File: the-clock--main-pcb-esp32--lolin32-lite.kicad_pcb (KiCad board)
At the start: 2 copper layers, 101.6 x 38.1 mm, 19 parts, among them J1 Conn_01x04, SW1 SW_Push, SW2 SW_Push, SW3 SW_Push, SW4 SW_Push

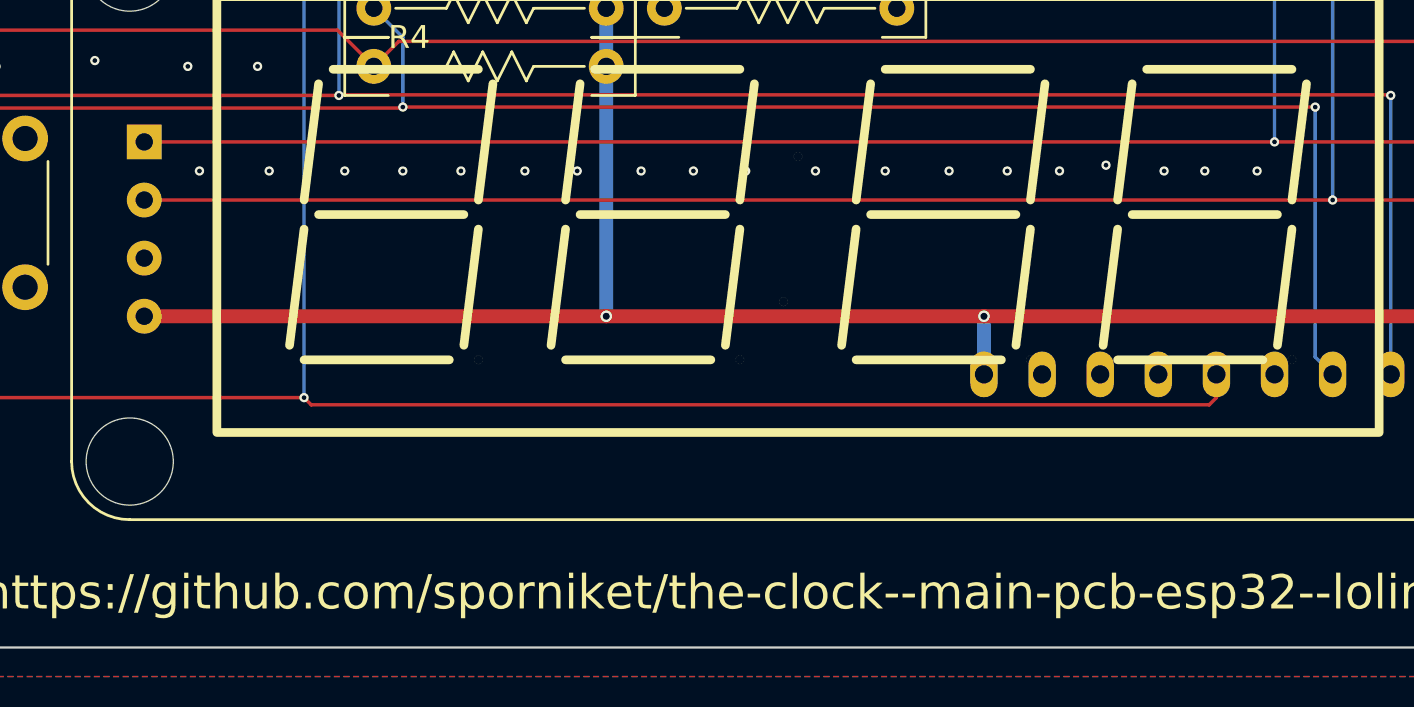
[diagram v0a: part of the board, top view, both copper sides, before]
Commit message: Fixed : missing pull-up resistors for SDA/SCL
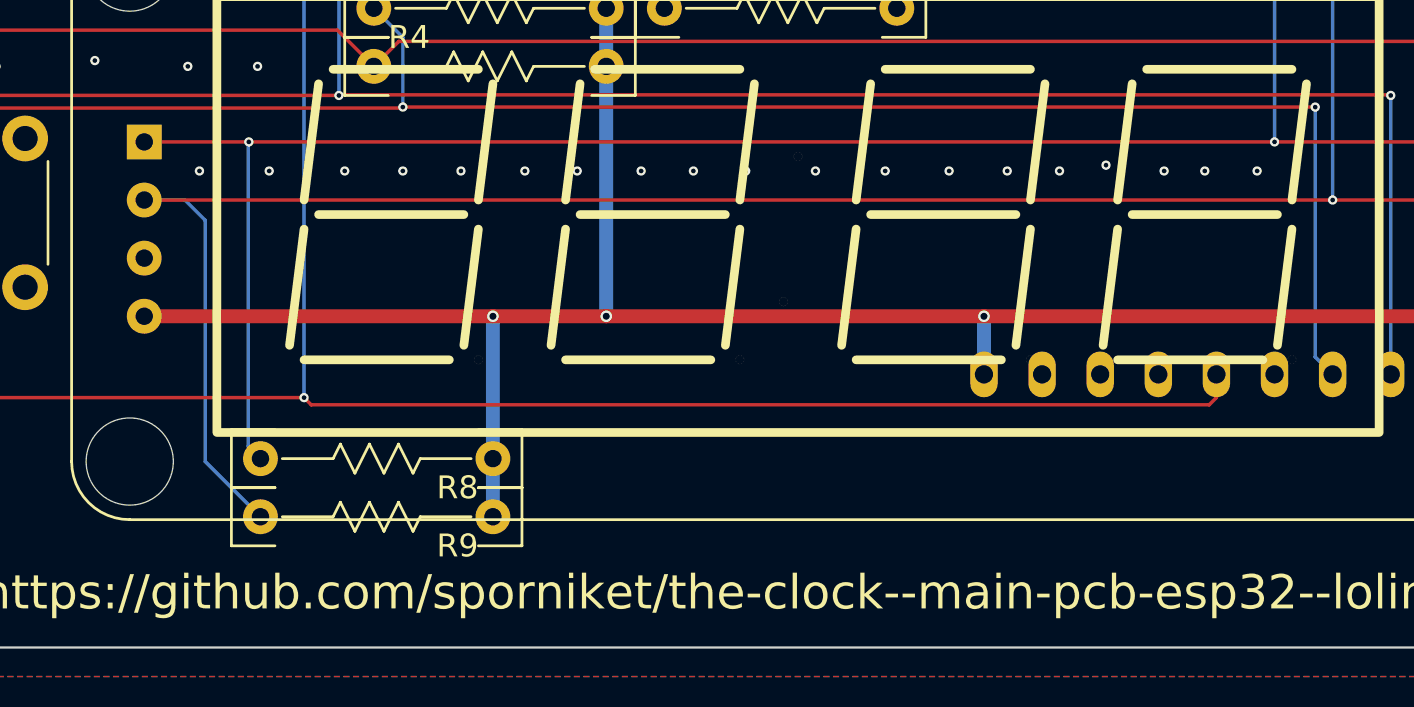
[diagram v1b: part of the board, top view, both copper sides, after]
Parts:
- added R8: 270, commons-passives_THT:Passive_THT_resistor_W2.54mm_L10.16mm, F.Cu at (83.9, 80.6)
- added R9: 270, commons-passives_THT:Passive_THT_resistor_W2.54mm_L10.16mm, F.Cu at (83.9, 83.2)
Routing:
- net /SDA: track 72.4 -> 89.4 mm
- net /SCL: track 69.9 -> 83.9 mm, vias 1 -> 2
- net VCC: track 80.8 -> 89.5 mm, vias 2 -> 3
